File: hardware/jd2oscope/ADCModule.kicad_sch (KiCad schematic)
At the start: 16 parts, among them J2 CONBNC001, U6 OPA192IDBVR, U7 ADS7279IPW

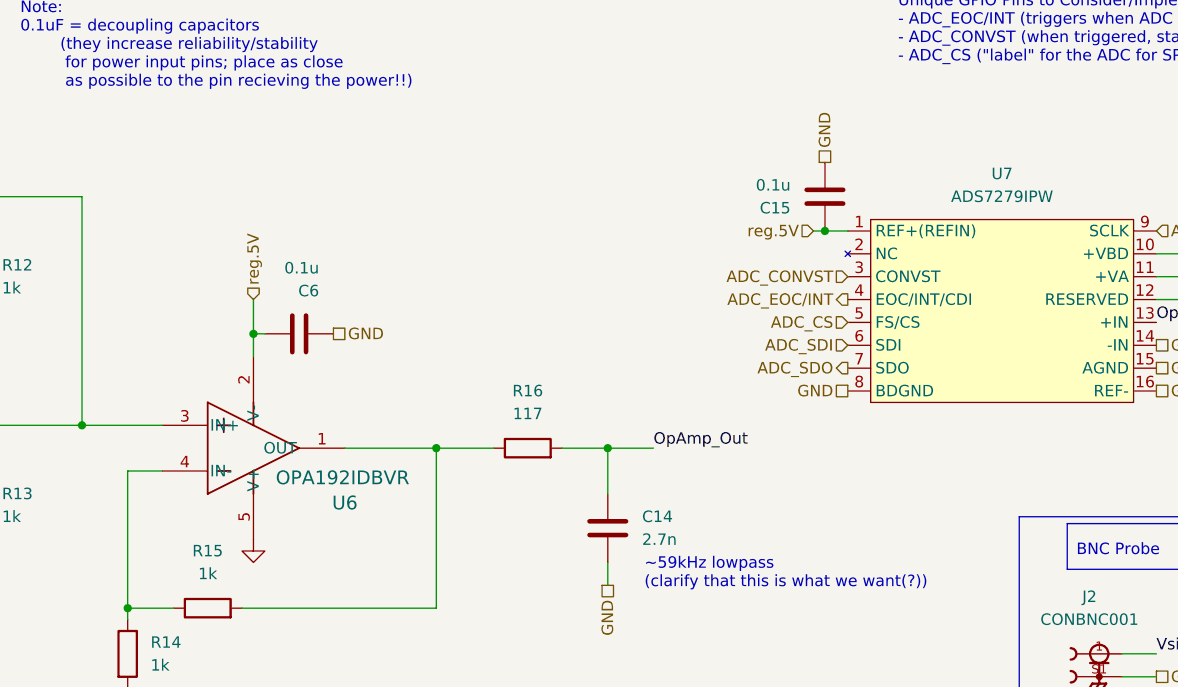
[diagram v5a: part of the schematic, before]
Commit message: fix: ERC funtimes
fixed a bunch of dependencies with ERC checks for the schematic; shouuuuld be easier/actually possible to open on other devices now?? (added a buncha schematics & footprints to the local files & whatnot)
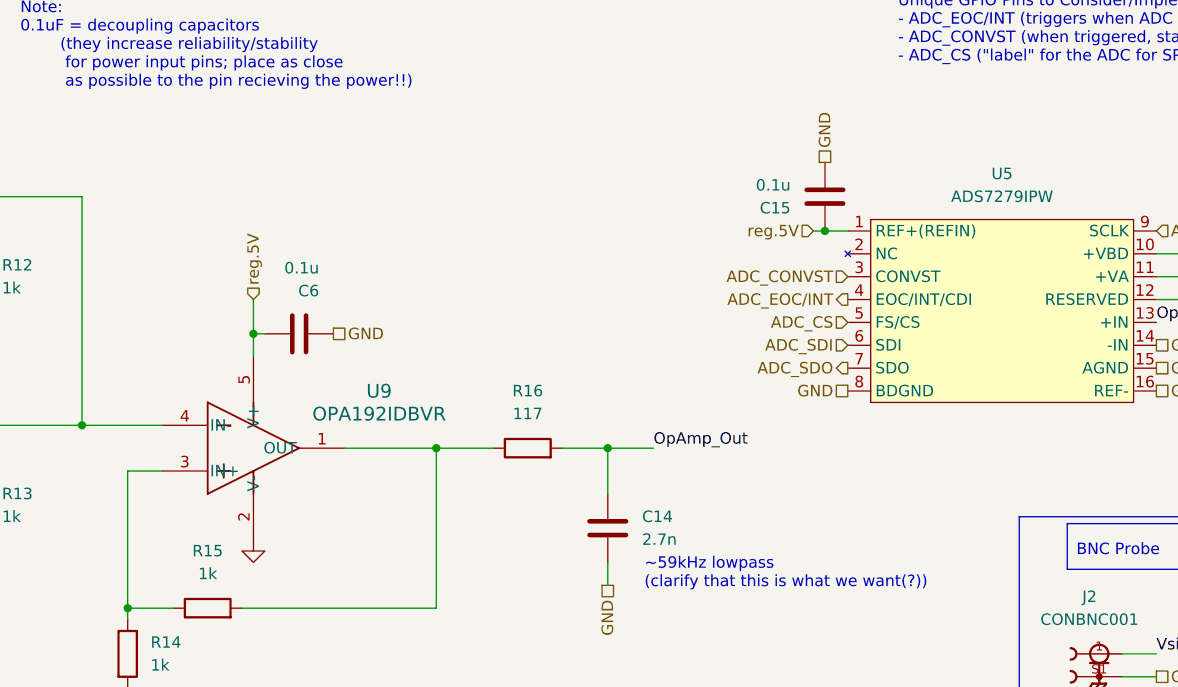
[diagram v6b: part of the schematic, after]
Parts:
- removed U6: OPA192IDBVR, pot:SOT95P280X145-5N, symbol Op-amp:OPA192IDBVR
- removed U7: ADS7279IPW, Package_CSP:LFCSP-16-1EP_4x4mm_P0.65mm_EP2.6x2.6mm, symbol ADS7279:ADS7279IPW
- added U5: ADS7279IPW, Package_CSP:LFCSP-16-1EP_4x4mm_P0.65mm_EP2.6x2.6mm, symbol ADS7279IPW:ADS7279IPW
- added U9: OPA192IDBVR, jd2Oscope_Footprints:SOT95P280X145-5N, symbol OPA192IDBVR:OPA192IDBVR
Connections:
- net ADC_CONVST: now also U5.3 (CONVST)
- net ADC_CS: now also U5.5 (FS/CS)
- net ADC_EOC/INT: now also U5.4 (EOC/INT/CDI)
- net ADC_SCK: now also U5.9 (SCLK)
- net ADC_SDI: now also U5.6 (SDI)
- net ADC_SDO: now also U5.7 (SDO)
- net GND: now also U5.14 (-IN), U5.15 (AGND), U5.16 (REF-), U5.8 (BDGND), U9.2 (V-)
- net OpAmp_Out: now also U5.13 (+IN)
- net reg.5V: now also U5.1 (REF+(REFIN)), U5.10 (+VBD), U5.11 (+VA), U5.12 (RESERVED), U9.5 (V+)
- net at R14.1, R15.1: now also U9.3 (IN+)
- net at R15.2, R16.1: now also U9.1 (OUT)
- net at R11.1, R12.1, R13.1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: now also U9.4 (IN-)

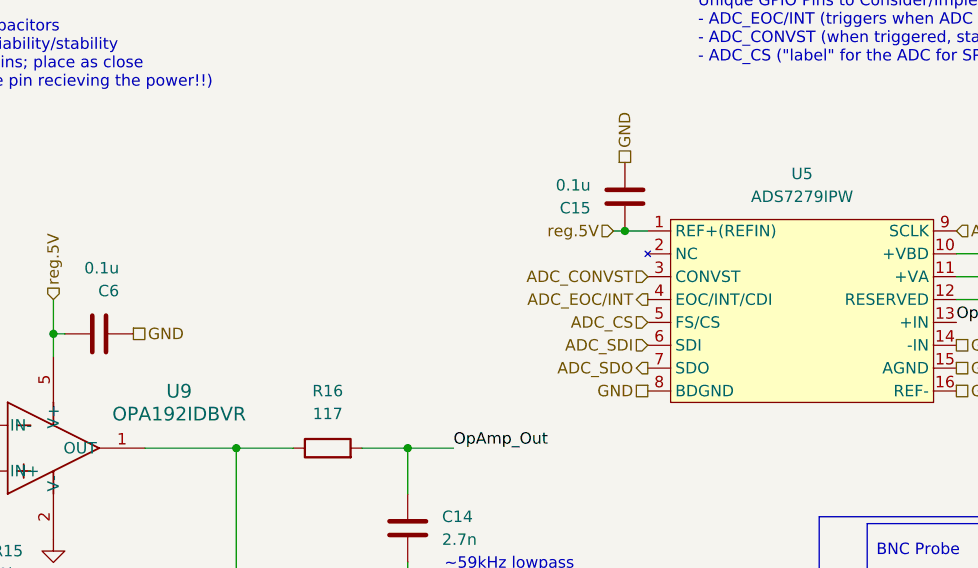
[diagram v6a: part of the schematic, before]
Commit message: fix: footprint/symbol fixes for ILI9341_Touch
blegh
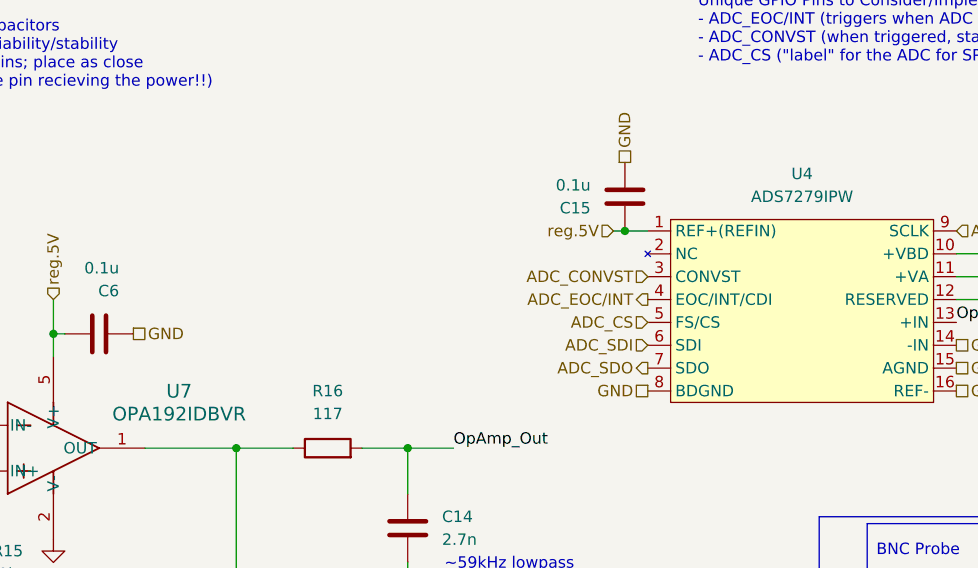
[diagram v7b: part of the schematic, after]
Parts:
- renumbered U5 to U4, U9 to U7
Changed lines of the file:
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@@
 		(dnp no)
 		(fields_autoplaced yes)
-		(property "Reference" "U9"
+		(property "Reference" "U7"
 			(at 90.17 59.7214 0)
 			(effects
@@
 		(dnp no)
 		(fields_autoplaced yes)
-		(property "Reference" "U5"
+		(property "Reference" "U4"
 			(at 159.385 35.56 0)
 			(effects

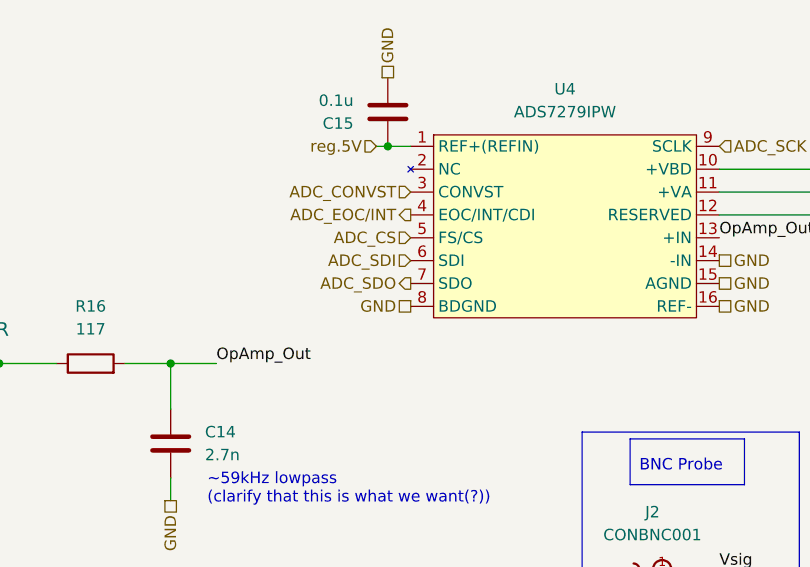
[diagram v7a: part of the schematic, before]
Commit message: feat: ERC is now happy!
We now pass all ERC checks in terms of errors; it is now fully satisfied!! (and, any warnings are just due to the fact that we made local edits to global symbol values, so we're ballin' all the way frfr)
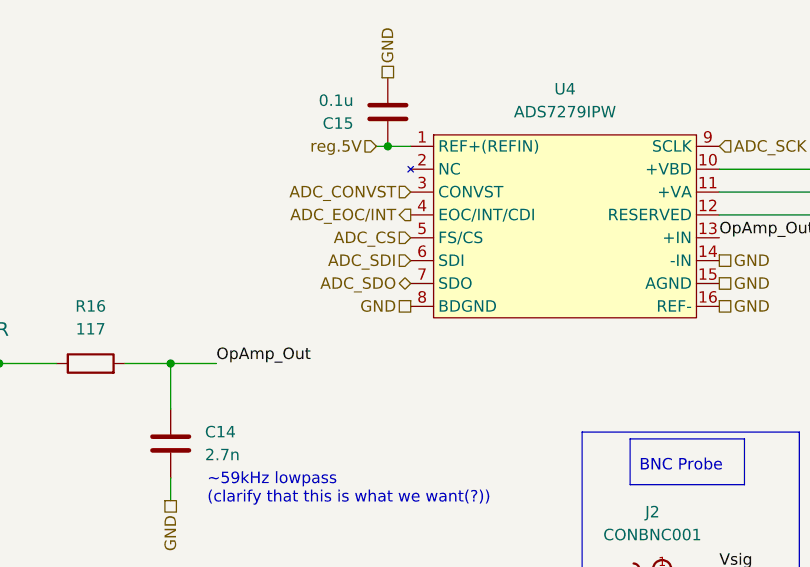
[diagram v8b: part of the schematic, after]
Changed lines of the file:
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@@
 	)
 	(hierarchical_label "ADC_SDO"
-		(shape output)
+		(shape tri_state)
 		(at 142.24 57.15 180)
 		(effects
